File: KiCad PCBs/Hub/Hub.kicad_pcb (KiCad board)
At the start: 2 copper layers, 175.3 x 29.2 mm, 23 parts, among them J1 Conn_02x04_Top_Bottom, J2 Conn_02x04_Top_Bottom, U2 RJ45-B-1*4, U3 RJ45-B-1*4

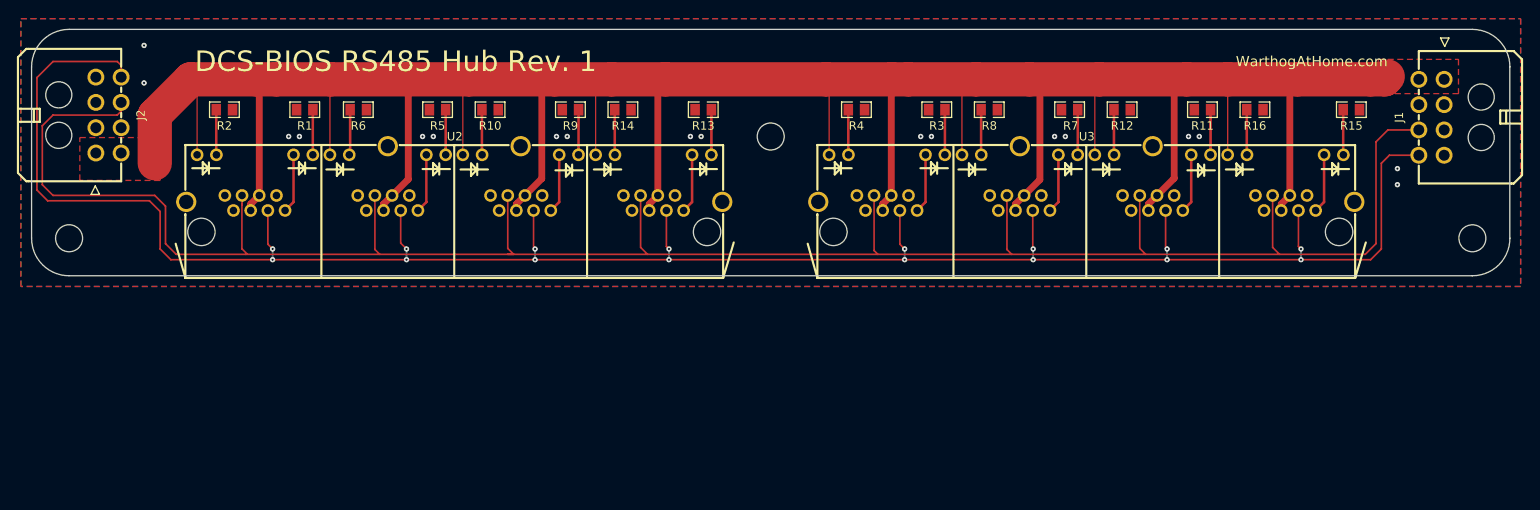
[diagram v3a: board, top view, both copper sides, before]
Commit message: Added some more silkscreen info to Hub
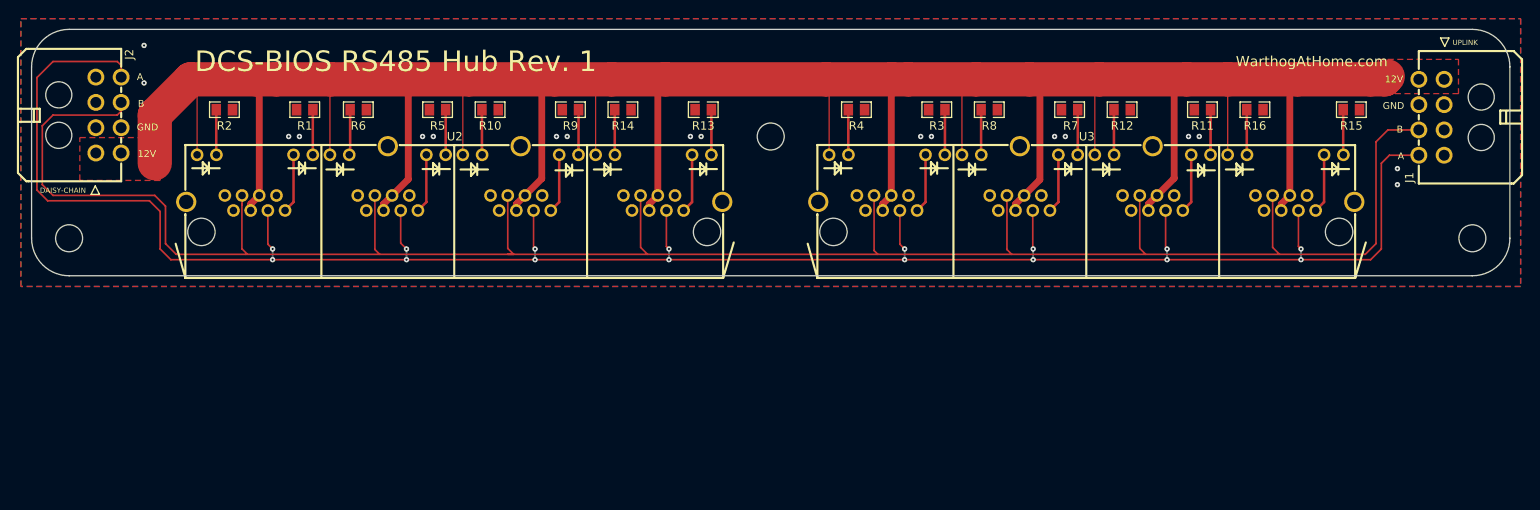
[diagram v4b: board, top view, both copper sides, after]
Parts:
- R1, R11, R13, R15, R3, R5, R7, R9: value 390R -> 1K
- R10, R12, R14, R16, R2, R4, R6, R8: value 1.8K -> 4.5K
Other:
- board text added: "1 PLED"
- board text added: "12V"
- board text added: "3 A"
- board text added: "5 12V"
- board text added: "6 B"
- board text added: "7 GND"
- board text added: "8 GND"
- board text added: "A"
- board text added: "B"
- board text added: "GND"

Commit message: Updated HUB LEDs
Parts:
- added D1: BLUE, LED_SMD:LED_0603_1608Metric, F.Cu at (220.3, 106.0)
- added R17: 1.8K, A10 KiCad Libraries:R0805, F.Cu at (222.9, 106.0)
- R10, R12, R14, R16, R2, R4, R6, R8: value 4.5K -> 1K
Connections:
- net 5V_S1 renamed PLED1
- net 5V_S2 renamed PLED2
- net 5V_S3 renamed PLED3
- net 5V_S4 renamed PLED4
- net 5V_S5 renamed PLED5
- net 5V_S6 renamed PLED6
- net 5V_S7 renamed PLED7
- net 5V_S8 renamed PLED8
- U2 pad 12: 12V -> ACT1
- U2 pad 14: unconnected-(U2-Pad14) -> ACT2
- U2 pad 2: unconnected-(U2-Pad2) -> ACT1
- U2 pad 24: 12V -> ACT2
- U2 pad 26: unconnected-(U2-Pad26) -> ACT3
- U2 pad 36: 12V -> ACT3
- U2 pad 38: unconnected-(U2-Pad38) -> ACT4
- U2 pad 48: 12V -> ACT4
- U3 pad 12: 12V -> ACT5
- U3 pad 14: unconnected-(U3-Pad14) -> ACT6
- U3 pad 2: unconnected-(U3-Pad2) -> ACT5
- U3 pad 24: 12V -> ACT6
- U3 pad 26: unconnected-(U3-Pad26) -> ACT7
- U3 pad 36: 12V -> ACT7
- U3 pad 38: unconnected-(U3-Pad38) -> ACT8
- U3 pad 48: 12V -> ACT8
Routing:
- net 12V: track 365.6 -> 313.0 mm
- net ACT1: track 0.00 -> 13.2 mm, vias 0 -> 2
- net ACT5: track 0.00 -> 13.2 mm, vias 0 -> 2
- net ACT4: track 0.00 -> 13.2 mm, vias 0 -> 2
- net ACT2: track 0.00 -> 13.2 mm, vias 0 -> 1
- net ACT8: track 0.00 -> 13.2 mm, vias 0 -> 2
- net ACT6: track 0.00 -> 12.8 mm, vias 0 -> 1
- net ACT7: track 0.00 -> 12.8 mm, vias 0 -> 1
- net ACT3: track 0.00 -> 12.8 mm, vias 0 -> 1
- net Net-(R17-Pad2): track 0.00 -> 2.62 mm
- net GND: vias 18 -> 36
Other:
- board text added: "1"
- board text added: "12V POWER"
- board text added: "2"
- board text added: "3"
- board text added: "4"
- board text added: "5"
- board text added: "6"
- board text added: "7"
- board text added: "8"

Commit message: Tweaked Hub
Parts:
- moved R17 3.07 mm to (221.6, 103.3), turned to 180 degrees
- moved D1 1.30 mm to (221.6, 105.8), turned to 180 degrees
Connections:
- net 12V renamed +12V
- net ACT1 renamed RX_LED1
- net ACT2 renamed RX_LED2
- net ACT3 renamed RX_LED3
- net ACT4 renamed RX_LED4
- net ACT5 renamed RX_LED5
- net ACT6 renamed RX_LED6
- net ACT7 renamed RX_LED7
- net ACT8 renamed RX_LED8
- net PLED1 renamed TX_LED1
- net PLED2 renamed TX_LED2
- net PLED3 renamed TX_LED3
- net PLED4 renamed TX_LED4
- net PLED5 renamed TX_LED5
- net PLED6 renamed TX_LED6
- net PLED7 renamed TX_LED7
- net PLED8 renamed TX_LED8
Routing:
- net GND: vias 36 -> 98
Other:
- board text added: "12V 5"
- board text added: "2 RX LED"
- board text added: "A 3"
- board text added: "GND 7"
- board text added: "TX LED 1"
- board text removed: "1 PLED"
- board text removed: "3 A"
- board text removed: "7 GND"

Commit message: Updated TX/RX resistors to 1.8K
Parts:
- R1, R10, R11, R12, R13, R14, R15, R16, R2, R3, R4, R5, R6, R7, R8, R9: value 1K -> 1.8K
- R17: value 1.8K -> 4.7K
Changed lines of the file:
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@@
     (descr "R0805 footprint")
     (tags "R0805 footprint")
-    (property "LCSC" "C17513")
+    (property "LCSC" "C17398")
     (property "Sheetfile" "Hub.kicad_sch")
     (property "Sheetname" "")
@@
       (effects (font (size 0.8128 0.8128) (thickness 0.127)))
     )
-    (fp_text value "1K" (at 0 2.917094) (layer "F.Fab")
+    (fp_text value "1.8K" (at 0 2.917094) (layer "F.Fab")
       (effects (font (size 1 1) (thickness 0.15)))
     )
@@
     (descr "R0805 footprint")
     (tags "R0805 footprint")
-    (property "LCSC" "C17513")
+    (property "LCSC" "C17398")
     (property "Sheetfile" "Hub.kicad_sch")
     (property "Sheetname" "")
@@
       (effects (font (size 0.8128 0.8128) (thickness 0.127)))
     )
-    (fp_text value "1K" (at 0 2.917094) (layer "F.Fab")
+    (fp_text value "1.8K" (at 0 2.917094) (layer "F.Fab")
       (effects (font (size 1 1) (thickness 0.15)))
     )
@@
     (descr "R0805 footprint")
     (tags "R0805 footprint")
-    (property "LCSC" "C17513")
+    (property "LCSC" "C17398")
     (property "Sheetfile" "Hub.kicad_sch")
     (property "Sheetname" "")
@@
       (effects (font (size 0.8128 0.8128) (thickness 0.127)))
     )
-    (fp_text value "1K" (at 0 2.917094) (layer "F.Fab")
+    (fp_text value "1.8K" (at 0 2.917094) (layer "F.Fab")
       (effects (font (size 1 1) (thickness 0.15)))
     )
@@
     (descr "R0805 footprint")
     (tags "R0805 footprint")
-    (property "LCSC" "C17513")
+    (property "LCSC" "C17398")
     (property "Sheetfile" "Hub.kicad_sch")
     (property "Sheetname" "")
@@
       (effects (font (size 0.8128 0.8128) (thickness 0.127)))
     )
-    (fp_text value "1K" (at 0 2.917094) (layer "F.Fab")
+    (fp_text value "1.8K" (at 0 2.917094) (layer "F.Fab")
       (effects (font (size 1 1) (thickness 0.15)))
     )
@@
     (descr "R0805 footprint")
     (tags "R0805 footprint")
-    (property "LCSC" "C17513")
+    (property "LCSC" "C17398")
     (property "Sheetfile" "Hub.kicad_sch")
     (property "Sheetname" "")
@@
       (effects (font (size 0.8128 0.8128) (thickness 0.127)))
     )
-    (fp_text value "1K" (at 0 2.917094) (layer "F.Fab")
+    (fp_text value "1.8K" (at 0 2.917094) (layer "F.Fab")
       (effects (font (size 1 1) (thickness 0.15)))
     )
@@
     (descr "R0805 footprint")
     (tags "R0805 footprint")
-    (property "LCSC" "C17513")
+    (property "LCSC" "C17398")
     (property "Sheetfile" "Hub.kicad_sch")
     (property "Sheetname" "")
@@
       (effects (font (size 0.8128 0.8128) (thickness 0.127)))
     )
-    (fp_text value "1K" (at 0 2.917094) (layer "F.Fab")
+    (fp_text value "1.8K" (at 0 2.917094) (layer "F.Fab")
       (effects (font (size 1 1) (thickness 0.15)))
     )
@@
     (descr "R0805 footprint")
     (tags "R0805 footprint")
-    (property "LCSC" "C17513")
+    (property "LCSC" "C17398")
     (property "Sheetfile" "Hub.kicad_sch")
     (property "Sheetname" "")
@@
       (effects (font (size 0.8128 0.8128) (thickness 0.127)))
     )
-    (fp_text value "1K" (at 0 2.917094) (layer "F.Fab")
+    (fp_text value "1.8K" (at 0 2.917094) (layer "F.Fab")
       (effects (font (size 1 1) (thickness 0.15)))
     )
@@
     (descr "R0805 footprint")
     (tags "R0805 footprint")
-    (property "LCSC" "C17513")
+    (property "LCSC" "C17398")
     (property "Sheetfile" "Hub.kicad_sch")
     (property "Sheetname" "")
@@
       (effects (font (size 0.8128 0.8128) (thickness 0.127)))
     )
-    (fp_text value "1K" (at 0 2.917094) (layer "F.Fab")
+    (fp_text value "1.8K" (at 0 2.917094) (layer "F.Fab")
       (effects (font (size 1 1) (thickness 0.15)))
     )
@@
     (descr "R0805 footprint")
     (tags "R0805 footprint")
-    (property "LCSC" "C17513")
+    (property "LCSC" "C17398")
     (property "Sheetfile" "Hub.kicad_sch")
     (property "Sheetname" "")
@@
       (effects (font (size 0.8128 0.8128) (thickness 0.127)))
     )
-    (fp_text value "1K" (at 0 2.917094) (layer "F.Fab")
+    (fp_text value "1.8K" (at 0 2.917094) (layer "F.Fab")
       (effects (font (size 1 1) (thickness 0.15)))
     )
@@
     (descr "R0805 footprint")
     (tags "R0805 footprint")
-    (property "LCSC" "C17398")
+    (property "LCSC" "C17673")
     (property "Sheetfile" "Hub.kicad_sch")
     (property "Sheetname" "")
@@
       (effects (font (size 0.5588 0.5588) (thickness 0.1016)))
     )
-    (fp_text value "1.8K" (at 0 2.917094) (layer "F.Fab")
+    (fp_text value "4.7K" (at 0 2.917094) (layer "F.Fab")
       (effects (font (size 1 1) (thickness 0.15)))
     )
@@
     (descr "R0805 footprint")
     (tags "R0805 footprint")
-    (property "LCSC" "C17513")
+    (property "LCSC" "C17398")
     (property "Sheetfile" "Hub.kicad_sch")
     (property "Sheetname" "")
@@
       (effects (font (size 0.8128 0.8128) (thickness 0.127)))
     )
-    (fp_text value "1K" (at 0 2.917094) (layer "F.Fab")
+    (fp_text value "1.8K" (at 0 2.917094) (layer "F.Fab")
       (effects (font (size 1 1) (thickness 0.15)))
     )
@@
     (descr "R0805 footprint")
     (tags "R0805 footprint")
-    (property "LCSC" "C17513")
+    (property "LCSC" "C17398")
     (property "Sheetfile" "Hub.kicad_sch")
     (property "Sheetname" "")
@@
       (effects (font (size 0.8128 0.8128) (thickness 0.127)))
     )
-    (fp_text value "1K" (at 0 2.917094) (layer "F.Fab")
+    (fp_text value "1.8K" (at 0 2.917094) (layer "F.Fab")
       (effects (font (size 1 1) (thickness 0.15)))
     )
@@
     (descr "R0805 footprint")
     (tags "R0805 footprint")
-    (property "LCSC" "C17513")
+    (property "LCSC" "C17398")
     (property "Sheetfile" "Hub.kicad_sch")
     (property "Sheetname" "")
@@
       (effects (font (size 0.8128 0.8128) (thickness 0.127)))
     )
-    (fp_text value "1K" (at 0 2.917094) (layer "F.Fab")
+    (fp_text value "1.8K" (at 0 2.917094) (layer "F.Fab")
       (effects (font (size 1 1) (thickness 0.15)))
     )
@@
     (descr "R0805 footprint")
     (tags "R0805 footprint")
-    (property "LCSC" "C17513")
+    (property "LCSC" "C17398")
     (property "Sheetfile" "Hub.kicad_sch")
     (property "Sheetname" "")
@@
       (effects (font (size 0.8128 0.8128) (thickness 0.127)))
     )
-    (fp_text value "1K" (at 0 2.917094) (layer "F.Fab")
+    (fp_text value "1.8K" (at 0 2.917094) (layer "F.Fab")
       (effects (font (size 1 1) (thickness 0.15)))
     )
@@
     (descr "R0805 footprint")
     (tags "R0805 footprint")
-    (property "LCSC" "C17513")
+    (property "LCSC" "C17398")
     (property "Sheetfile" "Hub.kicad_sch")
     (property "Sheetname" "")
@@
       (effects (font (size 0.8128 0.8128) (thickness 0.127)))
     )
-    (fp_text value "1K" (at 0 2.917094) (layer "F.Fab")
+    (fp_text value "1.8K" (at 0 2.917094) (layer "F.Fab")
       (effects (font (size 1 1) (thickness 0.15)))
     )
@@
     (descr "R0805 footprint")
     (tags "R0805 footprint")
-    (property "LCSC" "C17513")
+    (property "LCSC" "C17398")
     (property "Sheetfile" "Hub.kicad_sch")
     (property "Sheetname" "")
@@
       (effects (font (size 0.8128 0.8128) (thickness 0.127)))
     )
-    (fp_text value "1K" (at 0 2.917094) (layer "F.Fab")
+    (fp_text value "1.8K" (at 0 2.917094) (layer "F.Fab")
       (effects (font (size 1 1) (thickness 0.15)))
     )
@@
     (descr "R0805 footprint")
     (tags "R0805 footprint")
-    (property "LCSC" "C17513")
+    (property "LCSC" "C17398")
     (property "Sheetfile" "Hub.kicad_sch")
     (property "Sheetname" "")
@@
       (effects (font (size 0.8128 0.8128) (thickness 0.127)))
     )
-    (fp_text value "1K" (at 0 2.917094) (layer "F.Fab")
-      (effects (font (size 1 1) (thickness 0.15)))
-    )
+    (fp_text value "1.8K" (at 0 2.917094) (layer "F.Fab")
+      (effects (font (size 1 1) (thickness 0.15)))
+    )
